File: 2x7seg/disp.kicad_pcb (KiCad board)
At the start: 2 copper layers, 35.6 x 30.5 mm, 9 parts, among them P1 CONN_01X08, P2 CONN_01X08, U1 TLC59282_REV

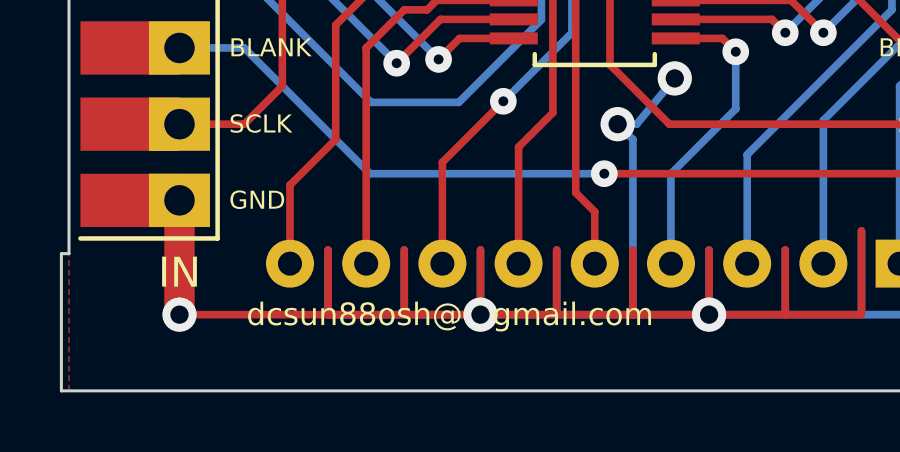
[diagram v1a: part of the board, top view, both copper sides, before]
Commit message: Update email address, regenerate gerber and plots. Change the sheet size of the clock power schematic page to A4.
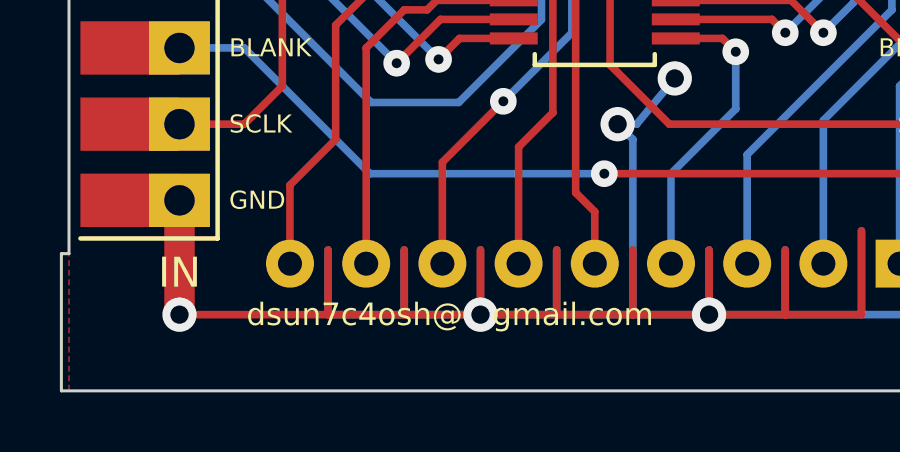
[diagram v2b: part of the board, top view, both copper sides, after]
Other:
- board text added: "dsun7c4osh@ gmail.com"
- board text removed: "dcsun88osh@ gmail.com"

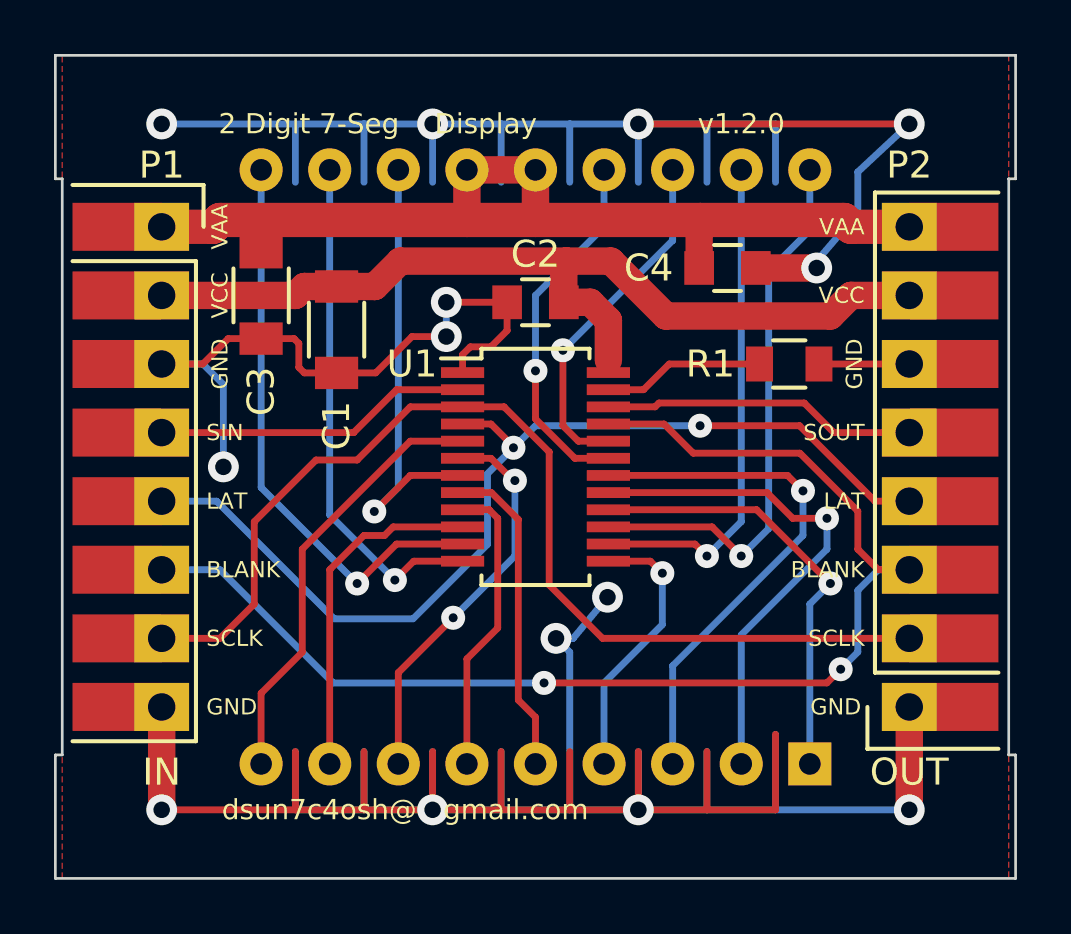
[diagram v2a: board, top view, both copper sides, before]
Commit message: Update 2x7seg design to KiCad 8.
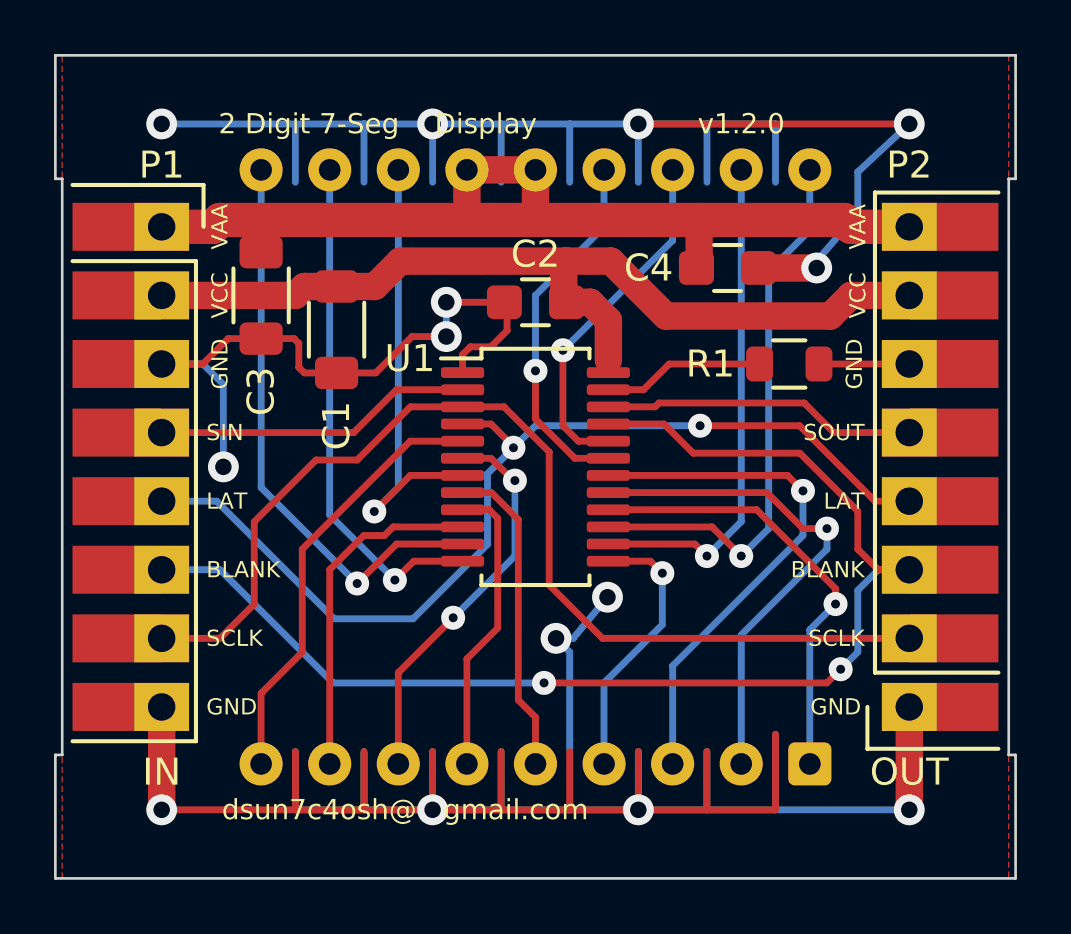
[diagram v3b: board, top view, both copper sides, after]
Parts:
- C1, C3: footprint local:C_1206_HandSoldering -> Local:C_1206_HandSoldering
- C2, C4: footprint local:C_0805_HandSoldering -> Local:C_0805_HandSoldering
- DS1: footprint local:LDD-A814RI -> Local:LDD-A814RI
- P1, P2: footprint local:Pin_Header_1x08_edge -> Local:Pin_Header_1x08_edge
- R1: footprint local:R_0805_HandSoldering -> Local:R_0805_HandSoldering
- U1: footprint local:SOIC-24_6.0x8.65mm_Pitch25mil -> Local:SSOP-24_3.9x8.65mm_Pitch0.635mm
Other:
- net class Default removed
- net class minimum removed
- rule pad_to_mask_clearance: 0 -> 0.0508
- rule solder_mask_min_width: 0.25 -> 0.1016

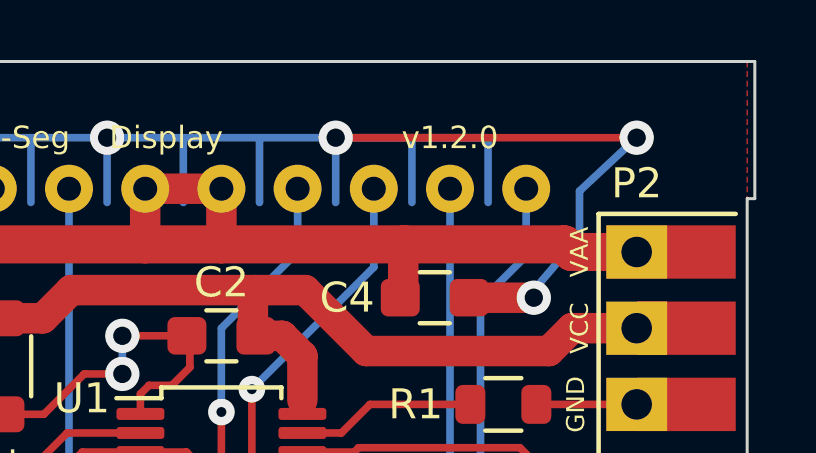
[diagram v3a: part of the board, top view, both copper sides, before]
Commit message: Bump version string of 2x7seg to v1.3.0.
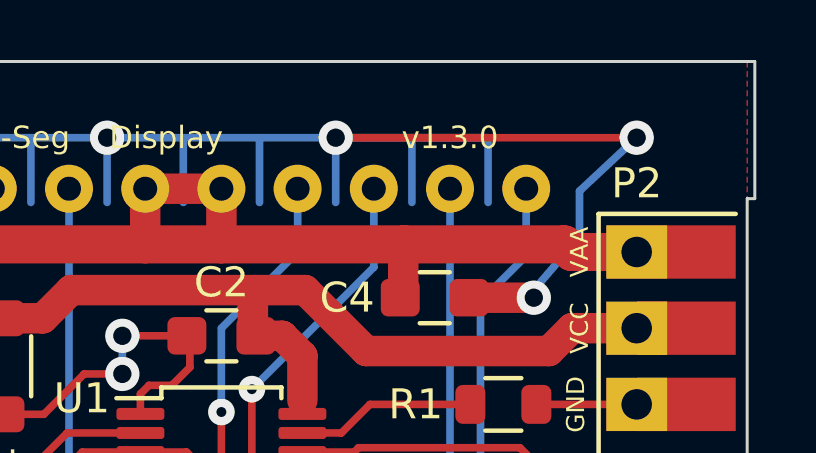
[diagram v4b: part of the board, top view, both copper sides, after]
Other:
- board text added: "v1.3.0"
- board text removed: "v1.2.0"
